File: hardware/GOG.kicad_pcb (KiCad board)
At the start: 2 copper layers, 100 x 100 mm, 129 parts, among them J1 USB_C_Receptacle_USB2.0_16P, J10 Conn_01x02, J11 Conn_01x02, J2 Conn_01x02_Pin, J3 Conn_01x04_Pin, J4 Conn_01x02_Pin, J5 85201239, J6 Conn_01x04_Pin, J7 Conn_01x04_Pin, J8 Screw_Terminal_01x02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

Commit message: design v1
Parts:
- moved TP_RESET1 56.3 mm to (112.0, 80.0)
- moved J5 50.6 mm to (106.8, 114.0), turned to -90 degrees
- moved C6 46.3 mm to (107.4, 104.9), turned to 90 degrees
- moved J11 45.2 mm to (191.5, 138.8)
- moved R13 44.1 mm to (180.8, 98.5)
- moved J7 42.1 mm to (195.2, 103.5)
- moved C5 41.9 mm to (110.2, 104.0), turned to 180 degrees
- moved TP22 41.7 mm to (178.5, 132.0)
- moved U3 41.4 mm to (118.5, 92.2), turned to -90 degrees
- moved R11 41.0 mm to (189.8, 86.1)
- moved R10 41.0 mm to (176.8, 98.4)
- moved R14 40.9 mm to (189.8, 89.9)
- moved R12 40.8 mm to (189.8, 88.0), turned to 180 degrees
- moved U4 40.8 mm to (178.8, 88.0)
- moved R9 40.7 mm to (110.2, 106.0), turned to 0 degrees
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- renumbered SW2 to BOOT, SW1 to EN
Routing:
- net GND: track 0.00 -> 737.3 mm, vias 0 -> 31
- net 3.3V: track 0.00 -> 231.9 mm, vias 0 -> 6
- net BQ_CE_N: track 0.00 -> 182.4 mm, vias 0 -> 3
- net VBUS: track 0.00 -> 146.4 mm, vias 0 -> 6
- net SCL: track 0.00 -> 138.2 mm, vias 0 -> 2
- net SDA: track 0.00 -> 127.9 mm, vias 0 -> 2
- net BQ_INT_N: track 0.00 -> 104.6 mm, vias 0 -> 6
- net VSYS: track 0.00 -> 67.8 mm, vias 0 -> 2
- net RFM_DIO0: track 0.00 -> 65.6 mm
- net Net-(Q3-S): track 0.00 -> 64.0 mm, vias 0 -> 2
- net Net-(U7-SW2): track 0.00 -> 62.7 mm, vias 0 -> 3
- net Net-(D3-K): track 0.00 -> 59.6 mm, vias 0 -> 2
- net SPI_SELECT: track 0.00 -> 57.8 mm, vias 0 -> 1
- net VBAT: track 0.00 -> 54.6 mm, vias 0 -> 2
- net EXTINT: track 0.00 -> 52.3 mm
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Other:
- board text added: "3.3"
- board text added: "EXTINT"
- board text added: "GND"
- board text added: "RX GPS"
- board text added: "RX TX"
- board text added: "SDA SCL"
- board text added: "SPI CLK"
- board text added: "SPI MISO"
- board text added: "SPI MOSI"
- board text added: "SPI SEL"
- board text added: "TP"
- board text added: "TX GPS"
- board text added: "VBAT"
- board text added: "~{reset}"
- board text added: "~{safe}"

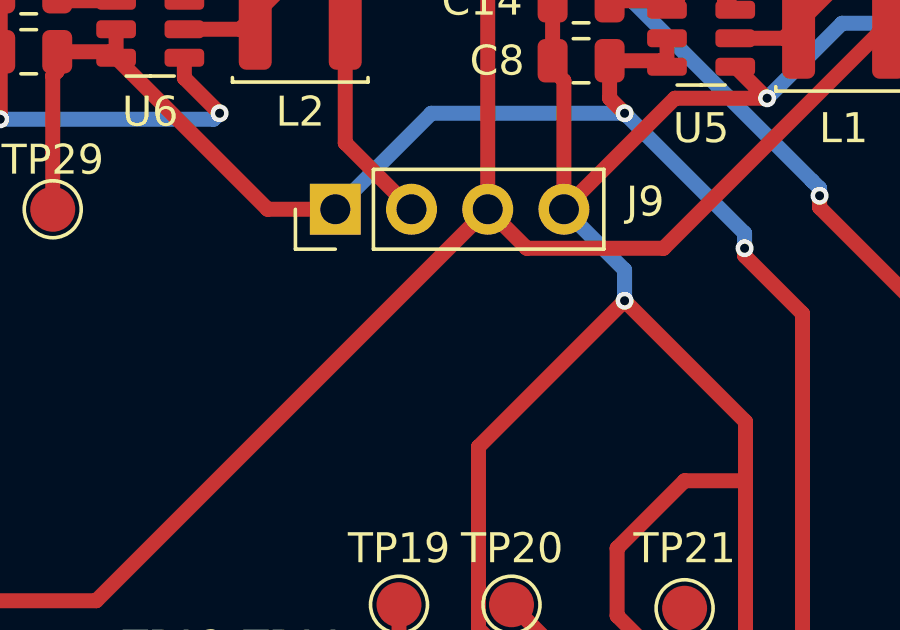
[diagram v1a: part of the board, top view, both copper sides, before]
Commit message: text for power pins add
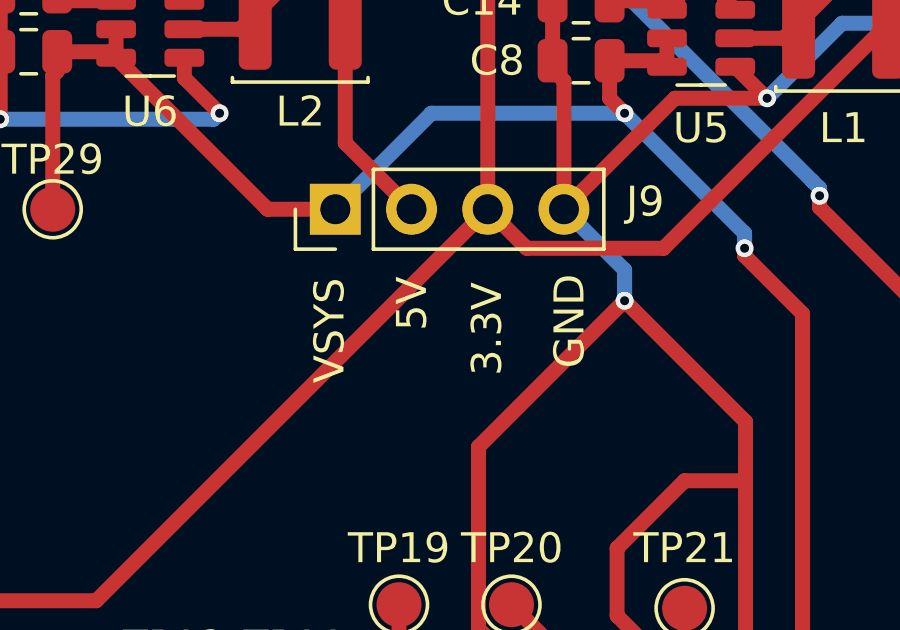
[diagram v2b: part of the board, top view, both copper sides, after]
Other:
- board text added: "3.3V"
- board text added: "5V"
- board text added: "VSYS"
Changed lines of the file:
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@@
+		)
+	)
+	(gr_text "3.3V"
+		(at 152.75 104.75 90)
+		(layer "F.SilkS")
+		(effects
+			(font
+				(size 1 1)
+				(thickness 0.15)
+			)
+			(justify left bottom)
 		)
 	)
@@
 	(gr_text "EXTINT"
 		(at 186.25 104.5 0)
+		(layer "F.SilkS")
+		(effects
+			(font
+				(size 1 1)
+				(thickness 0.15)
+			)
+			(justify left bottom)
+		)
+	)
+	(gr_text "VSYS"
+		(at 147.5 105 90)
 		(layer "F.SilkS")
 		(effects
@@
 		)
 	)
+	(gr_text "5V"
+		(at 150.25 103.25 90)
+		(layer "F.SilkS")
+		(effects
+			(font
+				(size 1 1)
+				(thickness 0.15)
+			)
+			(justify left bottom)
+		)
+	)
 	(gr_text "RX TX"
 		(at 163 70.25 0)
@@
 		(layer "F.SilkS")
 		(effects
+			(font
+				(size 1 1)
+				(thickness 0.15)
+			)
+			(justify left bottom)
+		)
+	)
+	(gr_text "GND"
+		(at 155.5 104.5 90)
+		(layer "F.SilkS")
+		(effects
